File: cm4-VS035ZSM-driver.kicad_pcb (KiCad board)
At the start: 2 copper layers, 19 parts, among them U201 TPS65131RGE, U202 TLV62568DBV

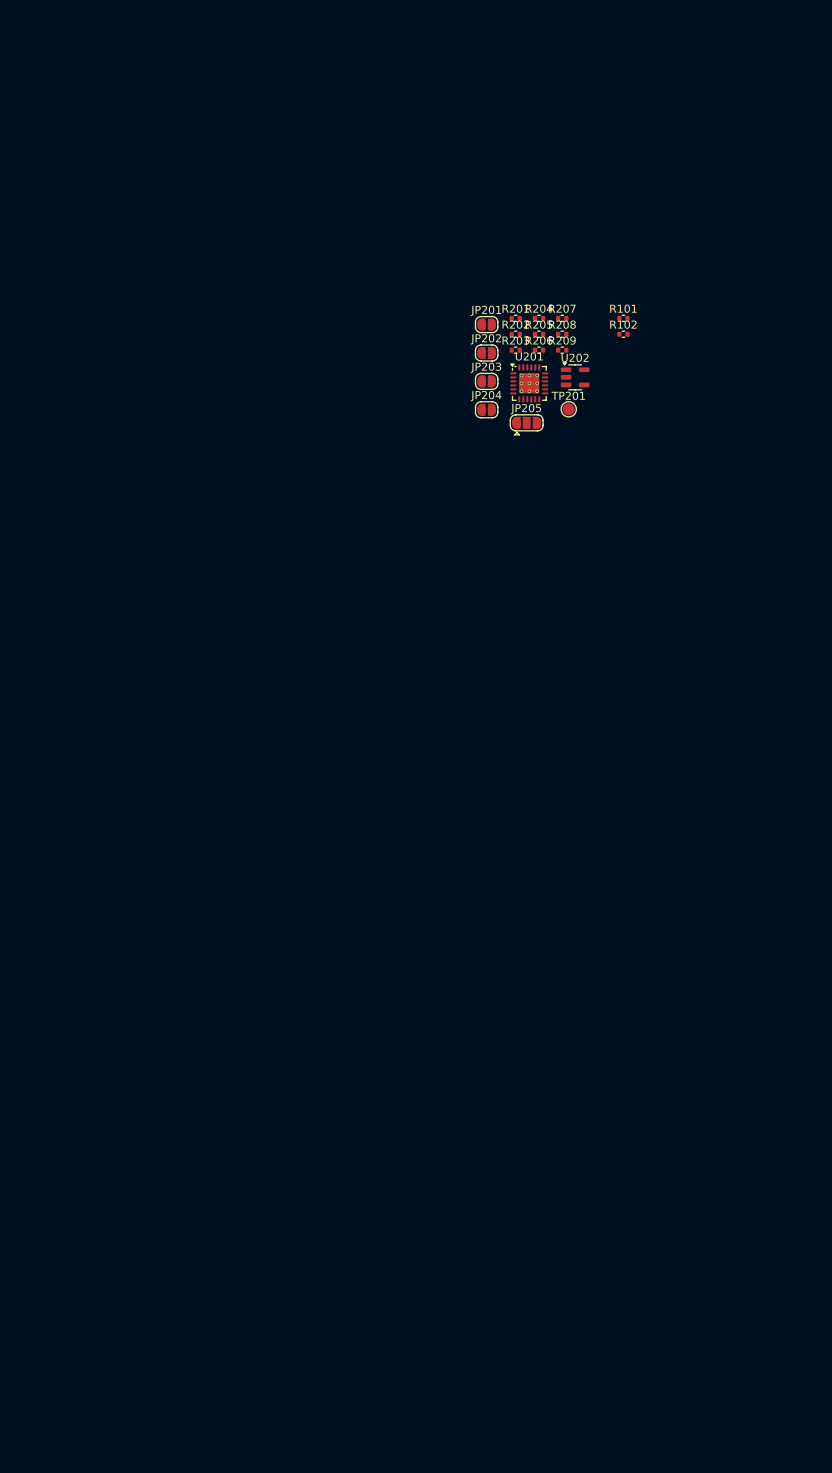
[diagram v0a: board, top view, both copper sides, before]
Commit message: 1v8 buck and 4.7uh inductor
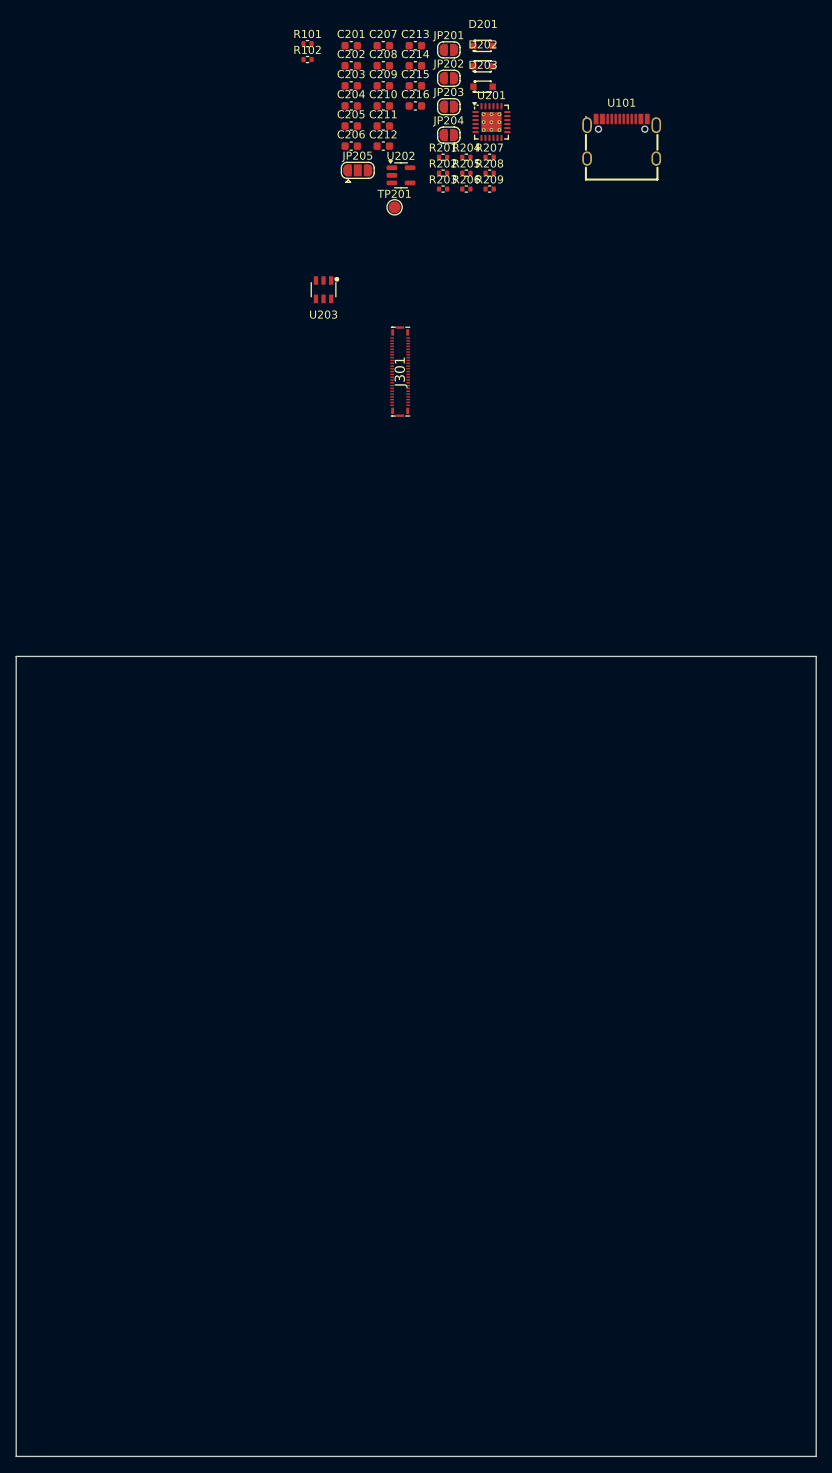
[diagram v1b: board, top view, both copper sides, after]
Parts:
- added C201: 10uF/25V, Capacitor_SMD:C_0603_1608Metric, F.Cu at (114.3, 44.3)
- added C202: 1uF/25V, Capacitor_SMD:C_0603_1608Metric, F.Cu at (114.3, 46.8)
- added C203: 10pF/25V, Capacitor_SMD:C_0603_1608Metric, F.Cu at (114.3, 49.3)
- added C204: 10uF/25V, Capacitor_SMD:C_0603_1608Metric, F.Cu at (114.3, 51.8)
- added C205: 10uF/25V, Capacitor_SMD:C_0603_1608Metric, F.Cu at (114.3, 54.4)
- added C206: 1uF/25V, Capacitor_SMD:C_0603_1608Metric, F.Cu at (114.3, 56.9)
- added C207: 10pF/25V, Capacitor_SMD:C_0603_1608Metric, F.Cu at (118.3, 44.3)
- added C208: 4.7nF/50V, Capacitor_SMD:C_0603_1608Metric, F.Cu at (118.3, 46.8)
- added C209: 10nF/25V, Capacitor_SMD:C_0603_1608Metric, F.Cu at (118.3, 49.3)
- added C210: 10uF/25V, Capacitor_SMD:C_0603_1608Metric, F.Cu at (118.3, 51.8)
- added C211: 10uF/25V, Capacitor_SMD:C_0603_1608Metric, F.Cu at (118.3, 54.4)
- added C212: 10uF/25V, Capacitor_SMD:C_0603_1608Metric, F.Cu at (118.3, 56.9)
- added C213: 6.8pF/10V, Capacitor_SMD:C_0603_1608Metric, F.Cu at (122.3, 44.3)
- added C214: 4.7uF/50V, Capacitor_SMD:C_0603_1608Metric, F.Cu at (122.3, 46.8)
- added C215: 2.2uF/50V, Capacitor_SMD:C_0603_1608Metric, F.Cu at (122.3, 49.3)
- added C216: 10uF/25V, Capacitor_SMD:C_0603_1608Metric, F.Cu at (122.3, 51.8)
- added D201: CUS10S40_H3F, footprints:SOD-323_L1.7-W1.3-LS2.5-RD, F.Cu at (130.7, 44.3)
- added D202: CUS10S40_H3F, footprints:SOD-323_L1.7-W1.3-LS2.5-RD, F.Cu at (130.7, 46.9)
- added D203: CUS10S40_H3F, footprints:SOD-323_L1.7-W1.3-LS2.5-RD, F.Cu at (130.7, 49.4)
- added J301: 245863050104829+, footprints:245863050104829, F.Cu at (120.4, 85.0)
- added U101: USB-TYPE-C-018, footprints:USB-C_SMD-TYPE-C-31-M-12, F.Cu at (148.1, 55.9)
- added U203: LP3320B6F, footprints:SOT-23-6_L2.9-W1.6-P0.95-LS2.8-BL, F.Cu at (110.8, 74.8)
- moved R101 52.3 mm to (108.8, 44.0)
- moved R102 52.3 mm to (108.8, 46.0)
- moved JP205 38.0 mm to (115.1, 59.9)
- moved JP201 34.7 mm to (126.5, 44.8)
- moved JP202 34.7 mm to (126.5, 48.4)
- moved JP203 34.7 mm to (126.5, 51.9)
- moved JP204 34.7 mm to (126.5, 55.5)
- moved TP201 33.3 mm to (119.7, 64.5)
- moved U202 33.3 mm to (120.5, 60.5)
- moved U201 33.0 mm to (131.8, 53.9)
- moved R203 22.1 mm to (125.8, 62.2)
- moved R206 22.1 mm to (128.7, 62.2)
- moved R209 22.1 mm to (131.6, 62.2)
- moved R201 22.1 mm to (125.8, 58.2)
- moved R204 22.1 mm to (128.7, 58.2)
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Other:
- board outline added: 100 x 100 mm

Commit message: init layout
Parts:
- removed C201, C204, C205, C210, C211: 10uF/25V, Capacitor_SMD:C_0603_1608Metric
- removed C202, C206: 1uF/25V, Capacitor_SMD:C_0603_1608Metric
- removed C203, C207: 10pF/25V, Capacitor_SMD:C_0603_1608Metric
- removed C208: 4.7nF/50V, Capacitor_SMD:C_0603_1608Metric
- removed C209: 10nF/25V, Capacitor_SMD:C_0603_1608Metric
- removed D201, D202, D203: CUS10S40_H3F, footprints:SOD-323_L1.7-W1.3-LS2.5-RD
- removed JP201: Jumper-, Jumper:SolderJumper-2_P1.3mm_Open_RoundedPad1.0x1.5mm
- removed JP202: Jumper+, Jumper:SolderJumper-2_P1.3mm_Open_RoundedPad1.0x1.5mm
- removed R101, R102: 5.1K, Resistor_SMD:R_0402_1005Metric
- removed R201: 10Ω/1%, Resistor_SMD:R_0402_1005Metric
- removed R202: 560kΩ/1%, Resistor_SMD:R_0402_1005Metric
- removed R203, R204: 150kΩ/1%, Resistor_SMD:R_0402_1005Metric
- removed R205: 715kΩ/1%, Resistor_SMD:R_0402_1005Metric
- removed R206: 100kΩ/1%, Resistor_SMD:R_0402_1005Metric
- removed R207: 200KΩ/1%, Resistor_SMD:R_0402_1005Metric
- removed U101: USB-TYPE-C-018, footprints:USB-C_SMD-TYPE-C-31-M-12
- removed U201: TPS65131RGE, Package_DFN_QFN:VQFN-24-1EP_4x4mm_P0.5mm_EP2.45x2.45mm_ThermalVias
- added C220: 4.7uF/16V, Capacitor_SMD:C_0603_1608Metric, F.Cu at (180.6, 55.0)
- added C221: 4.7uF/16V, Capacitor_SMD:C_0603_1608Metric, F.Cu at (185.1, 49.8)
- added C222: 4.7uF/16V, Capacitor_SMD:C_0603_1608Metric, F.Cu at (181.6, 47.1)
- added C223: 4.7uF/16V, Capacitor_SMD:C_0603_1608Metric, F.Cu at (178.2, 50.5)
- added D403: B5817WS_C7420329, footprints:SOD-323_L1.7-W1.3-LS2.5-FD, F.Cu at (185.3, 61.8)
- added J302: Conn_01x22, footprints:CON22_1X22_DRB_XF2C_TYC, F.Cu at (195.9, 70.4)
- added J303: Conn_01x02_LCD_Breakout, Connector_PinHeader_2.54mm:PinHeader_1x02_P2.54mm_Vertical, F.Cu at (205.6, 65.9)
- added J304: Conn_01x04_power_jumpers, Connector_PinHeader_2.54mm:PinHeader_1x04_P2.54mm_Vertical, F.Cu at (209.2, 71.0)
- added JP208: +5.7_bridge, Connector_PinHeader_2.54mm:PinHeader_1x02_P2.54mm_Vertical, F.Cu at (181.2, 60.2)
- added JP209: -5v7_bridge, Connector_PinHeader_2.54mm:PinHeader_1x02_P2.54mm_Vertical, F.Cu at (177.6, 57.6)
- added JP210: Jumper+, Connector_PinHeader_2.54mm:PinHeader_1x02_P2.54mm_Vertical, F.Cu at (188.4, 47.1)
- added JP211: Jumper-, Connector_PinHeader_2.54mm:PinHeader_1x02_P2.54mm_Vertical, F.Cu at (188.4, 55.8)
- added L204: 4.7uH, footprints:IND-SMD_L2.5-W2.0_SPH252012, F.Cu at (181.8, 66.6)
- added L206: 4.7uH, footprints:IND-SMD_L2.5-W2.0_SPH252012, F.Cu at (201.8, 42.3)
- added L207: 4.7uH, footprints:IND-SMD_L2.5-W2.0_SPH252012, F.Cu at (177.8, 47.1)
- added NT201: NetTie_GND, NetTie:NetTie-2_SMD_Pad0.5mm, B.Cu at (183.4, 44.8)
- added TP203: TestPoint_GND_PAD, TestPoint:TestPoint_THTPad_D2.0mm_Drill1.0mm, F.Cu at (195.1, 43.4)
- added TP204: TestPoint_GNDA_PAD, TestPoint:TestPoint_THTPad_D2.0mm_Drill1.0mm, F.Cu at (185.0, 46.9)
- added TP205: TestPoint_anode, TestPoint:TestPoint_THTPad_D2.0mm_Drill1.0mm, F.Cu at (177.6, 63.8)
- added TP206: TestPoint_cathode, TestPoint:TestPoint_THTPad_D2.0mm_Drill1.0mm, F.Cu at (186.2, 67.1)
- added TP207: TestPoint_PWM, TestPoint:TestPoint_THTPad_D2.0mm_Drill1.0mm, F.Cu at (177.8, 67.0)
- added TP208: TestPoint_P_5V7, TestPoint:TestPoint_THTPad_D2.0mm_Drill1.0mm, F.Cu at (186.6, 43.1)
- added TP209: TestPoint_N_5V7, TestPoint:TestPoint_THTPad_D2.0mm_Drill1.0mm, F.Cu at (185.0, 55.7)
- added U204: MCP1603T-180I/OS, footprints:TSOT5_MC_MCH, F.Cu at (205.6, 42.0)
- C212: value 10uF/25V -> 4.7uF/16V
- C213: value 6.8pF/10V -> 2.2uF/50V; footprint Capacitor_SMD:C_0603_1608Metric -> Capacitor_SMD:C_0805_2012Metric
- C214: value 4.7uF/50V -> 4.7uF/16V
- C215: footprint Capacitor_SMD:C_0603_1608Metric -> Capacitor_SMD:C_0805_2012Metric
- J301: footprint footprints:245863050104829 -> footprints:245863050104829_missing pads
- JP203, JP204: footprint Jumper:SolderJumper-2_P1.3mm_Open_RoundedPad1.0x1.5mm -> Connector_PinHeader_2.54mm:PinHeader_1x02_P2.54mm_Vertical
- JP205: footprint Jumper:SolderJumper-3_P1.3mm_Open_RoundedPad1.0x1.5mm -> Connector_PinHeader_2.54mm:PinHeader_1x03_P2.54mm_Vertical
- TP201: footprint TestPoint:TestPoint_Pad_D1.5mm -> TestPoint:TestPoint_THTPad_D2.0mm_Drill1.0mm
- U202: value TLV62568DBV -> TPS65132WRVCR_C2876379; footprint Package_TO_SOT_SMD:SOT-23-5 -> footprints:WQFN-20_L4.0-W3.0-P0.50-BL-EP
- moved TP201 91.5 mm to (207.5, 39.0), turned to 180 degrees
- moved C212 86.4 mm to (202.9, 39.7), turned to 180 degrees
- moved C214 86.2 mm to (208.4, 42.7), turned to -90 degrees
- moved JP204 85.9 mm to (210.9, 39.8)
- moved J301 82.6 mm to (196.3, 52.6)
- moved U203 73.6 mm to (183.7, 64.7), turned to 45 degrees
- moved JP203 73.0 mm to (198.6, 40.9)
- moved JP205 69.6 mm to (183.8, 70.7), turned to -90 degrees
- moved C215 65.8 mm to (186.5, 63.9), turned to -45 degrees
- moved C213 62.8 mm to (184.6, 52.2), turned to 90 degrees
- moved U202 61.5 mm to (181.2, 51.2), turned to -90 degrees
- moved C216 59.6 mm to (180.6, 64.1), turned to 45 degrees
- moved R209 55.7 mm to (186.6, 70.7), turned to 90 degrees
- moved R208 52.5 mm to (184.0, 61.1), turned to -135 degrees
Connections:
- net +5V renamed +3V3
- C213 pad 1: Net-(JP203-A) -> Net-(U202-CFLY2)
- C213 pad 2: Net-(U202-FB) -> Net-(U202-CFLY1)
- J301 pad 41: /high-speed/LED_PWR.A -> /MIPI-screen/LED_PWR.A
- J301 pad 45: /high-speed/LED_PWR.K -> /MIPI-screen/LED_PWR.K
- J301 pad 47: /high-speed/LED_PWR.K -> /MIPI-screen/LED_PWR.K
- J301 pad 48: /high-speed/LED_PWR.PWM -> /MIPI-screen/LED_PWR.PWM
- U202 pad 1: Net-(JP204-A) -> GND
- U202 pad 3: Net-(U202-SW) -> GNDA
- U202 pad 5: Net-(U202-FB) -> Net-(JP208-B)
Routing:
- net /high-speed/DSI0_DATA.3_N: track 0.00 -> 26.7 mm
- net /high-speed/DSI0_DATA.2_N: track 0.00 -> 26.5 mm
- net /high-speed/DSI0_DATA.0_N: track 0.00 -> 26.5 mm
- net /high-speed/DSI0_DATA.1_N: track 0.00 -> 26.5 mm
- net /high-speed/DSI0_CLK.N: track 0.00 -> 26.5 mm
- net /high-speed/DSI0_DATA.0_P: track 0.00 -> 26.2 mm
- net /high-speed/DSI0_DATA.1_P: track 0.00 -> 26.2 mm
- net /high-speed/DSI0_DATA.2_P: track 0.00 -> 26.0 mm
- net /high-speed/DSI0_CLK.P: track 0.00 -> 26.0 mm
- net /high-speed/DSI0_DATA.3_P: track 0.00 -> 25.6 mm
- net +3V3: track 0.00 -> 11.4 mm
- net GND: track 0.00 -> 7.66 mm
- net Net-(JP203-A): track 0.00 -> 4.16 mm
- net Net-(U202-CFLY2): track 0.00 -> 3.72 mm
- net /MIPI-screen/OUTP: track 0.00 -> 3.47 mm
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- added copper zone on F.Cu, net /MIPI-screen/SW
- added copper zone on B.Cu, net GND
- added copper zone on F.Cu, net GND
- added copper zone on In1.Cu, net GND
- added copper zone on In2.Cu, net GND
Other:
- board size 100 x 100 mm -> 37.6 x 35.5 mm
- copper layers 2 -> 4
- board text added: "good luck!"
- board text added: "it might be facing this way"

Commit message: silkscreen
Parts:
- added kibuzzard-685CA5E3: G***, kibuzzard-685CA5E3, F.Cu at (169.8, 57.6)
- added kibuzzard-685CA5ED: G***, kibuzzard-685CA5ED, F.Cu at (169.7, 59.6)
- added kibuzzard-685CA646: G***, kibuzzard-685CA646, F.Cu at (170.3, 62.0)
- added kibuzzard-685CA653: G***, kibuzzard-685CA653, F.Cu at (170.0, 64.1)
- added kibuzzard-685CA659: G***, kibuzzard-685CA659, F.Cu at (170.1, 65.8)
- added kibuzzard-685CA68D: G***, kibuzzard-685CA68D, F.Cu at (171.1, 50.6)
- added kibuzzard-685CA698: G***, kibuzzard-685CA698, F.Cu at (170.9, 48.8)
- added kibuzzard-685CA6CA: G***, kibuzzard-685CA6CA, F.Cu at (170.6, 42.8)
- added kibuzzard-685CA6D3: G***, kibuzzard-685CA6D3, F.Cu at (170.4, 41.0)
- added kibuzzard-685CA6E7: G***, kibuzzard-685CA6E7, F.Cu at (170.7, 34.7)
- added kibuzzard-685CA70B: G***, kibuzzard-685CA70B, F.Cu at (193.1, 36.0)
- added kibuzzard-685CA724: G***, kibuzzard-685CA724, F.Cu at (200.3, 36.0)
- added kibuzzard-685CA72C: G***, kibuzzard-685CA72C, F.Cu at (208.8, 36.2)
- moved TP201 12.6 mm to (195.0, 40.0)
- moved J303 4.55 mm to (209.5, 63.5)
- moved C213 3.87 mm to (184.6, 48.3)
- moved C222 3.87 mm to (181.6, 43.2)
- moved C220 3.87 mm to (180.6, 51.1)
- moved C221 3.87 mm to (185.1, 45.9)
- moved C223 3.87 mm to (178.2, 46.7)
- moved JP208 3.87 mm to (181.2, 56.3)
- moved JP209 3.87 mm to (177.6, 53.8)
- moved JP210 3.87 mm to (188.4, 43.2)
- moved JP211 3.87 mm to (188.4, 51.9)
- moved L207 3.87 mm to (177.8, 43.2)
- moved NT201 3.87 mm to (183.4, 40.9)
- moved TP204 3.87 mm to (185.0, 43.1)
- moved TP209 3.87 mm to (185.0, 51.8)
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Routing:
- net /high-speed/DSI0_DATA.3_P: track 25.6 -> 26.6 mm

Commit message: board fabbed
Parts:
- removed J303: Conn_01x02_LCD_Breakout, Connector_PinHeader_2.54mm:PinHeader_1x02_P2.54mm_Vertical
- removed R208: 100KΩ/1%, Resistor_SMD:R_0402_1005Metric
- added G***: LOGO, custom-graphics:isaac-anime-girl-2, F.Cu at (204.3, 47.9)
- added H305: MountingHole_Pad, MountingHole:MountingHole_3.2mm_M3_DIN965_Pad_TopBottom, F.Cu at (179.0, 37.5)
- added H307: MountingHole_Pad, MountingHole:MountingHole_3.2mm_M3_DIN965_Pad_TopBottom, F.Cu at (205.2, 36.7)
- added H308: MountingHole_Pad, MountingHole:MountingHole_3.2mm_M3_DIN965_Pad_TopBottom, F.Cu at (209.6, 70.0)
- added J305: Conn_01x03_Pin, Connector_PinHeader_2.54mm:PinHeader_1x03_P2.54mm_Vertical, F.Cu at (204.3, 64.8)
- added R206: 5.1Ω/1%, Resistor_SMD:R_0805_2012Metric, F.Cu at (179.6, 64.6)
- added R301: 2.2kΩ, Resistor_SMD:R_0402_1005Metric, F.Cu at (184.3, 59.1)
- added R302: 2.2kΩ, Resistor_SMD:R_0402_1005Metric, F.Cu at (187.0, 57.3)
- added R303: 2.2kΩ, Resistor_SMD:R_0402_1005Metric, F.Cu at (204.9, 71.5)
- added R304: 2.7kΩ, Resistor_SMD:R_0603_1608Metric, F.Cu at (204.7, 69.4)
- added REF**: sus-microsystems_amogus, custom-graphics:sus-microsystems_amogus, F.Cu at (194.0, 44.9)
- added REF**: sus-microsystems_amogus, custom-graphics:sus-microsystems_amogus, F.Cu at (184.0, 38.6)
- added kibuzzard-685CA5E3: G***, kibuzzard-685CA5E3, B.Cu at (186.9, 65.6)
- added kibuzzard-685CA5ED: G***, kibuzzard-685CA5ED, B.Cu at (183.5, 59.4)
- added kibuzzard-685CA646: G***, kibuzzard-685CA646, B.Cu at (180.2, 71.6)
- added kibuzzard-685CA653: G***, kibuzzard-685CA653, B.Cu at (177.6, 69.7)
- added kibuzzard-685CA659: G***, kibuzzard-685CA659, B.Cu at (182.8, 69.6)
- added kibuzzard-685CA68D: G***, kibuzzard-685CA68D, B.Cu at (177.2, 54.9)
- added kibuzzard-685CA698: G***, kibuzzard-685CA698, B.Cu at (184.6, 55.0)
- added kibuzzard-685CA6CA: G***, kibuzzard-685CA6CA, B.Cu at (189.4, 52.6)
- added kibuzzard-685CA6D3: G***, kibuzzard-685CA6D3, B.Cu at (186.5, 41.7)
- added kibuzzard-685CA6E7: G***, kibuzzard-685CA6E7, B.Cu at (181.2, 42.8)
- added kibuzzard-685CA70B: G***, kibuzzard-685CA70B, B.Cu at (194.6, 43.1)
- added kibuzzard-685CA724: G***, kibuzzard-685CA724, B.Cu at (200.0, 42.2)
- added kibuzzard-685CA72C: G***, kibuzzard-685CA72C, B.Cu at (209.5, 46.6)
- added kibuzzard-68620294: G***, kibuzzard-68620294, F.Cu at (204.2, 58.8)
- added kibuzzard-68620294: G***, kibuzzard-68620294, B.Cu at (204.1, 59.0)
- added kibuzzard-686202AB: G***, kibuzzard-686202AB, F.Cu at (209.8, 58.8)
- added kibuzzard-686202AB: G***, kibuzzard-686202AB, F.Cu at (192.3, 43.6)
- added kibuzzard-686202AB: G***, kibuzzard-686202AB, B.Cu at (209.4, 59.0)
- added kibuzzard-686202AB: G***, kibuzzard-686202AB, B.Cu at (191.7, 37.6)
- added kibuzzard-686202C6: G***, kibuzzard-686202C6, F.Cu at (202.1, 64.9)
- added kibuzzard-686202C6: G***, kibuzzard-686202C6, B.Cu at (202.4, 64.7)
- added kibuzzard-686202CD: G***, kibuzzard-686202CD, F.Cu at (205.7, 67.2)
- added kibuzzard-686202CD: G***, kibuzzard-686202CD, B.Cu at (206.8, 62.9)
- added kibuzzard-68621440: G***, kibuzzard-68621440, F.Cu at (211.7, 65.0)
- added kibuzzard-68621440: G***, kibuzzard-68621440, B.Cu at (211.4, 64.8)
- added kibuzzard-68621EB5: G***, kibuzzard-68621EB5, F.Cu at (197.0, 36.4)
- added kibuzzard-68622B0B: G***, kibuzzard-68622B0B, B.Cu at (195.7, 50.2)
- added kibuzzard-68622B1B: G***, kibuzzard-68622B1B, B.Cu at (200.7, 51.0)
- NT201: moved to F.Cu
- moved kibuzzard-685CA6CA 20.9 mm to (189.9, 50.8), turned to -90 degrees
- moved kibuzzard-685CA6D3 20.8 mm to (190.9, 44.5), turned to -90 degrees
- moved kibuzzard-685CA5E3 18.8 mm to (187.0, 65.3)
- moved kibuzzard-685CA5ED 17.4 mm to (187.0, 61.3)
- moved kibuzzard-685CA698 15.5 mm to (185.2, 54.9), turned to -90 degrees
- moved kibuzzard-685CA6E7 15.2 mm to (184.6, 40.8)
- moved kibuzzard-685CA646 14.1 mm to (180.5, 71.7)
- moved kibuzzard-685CA659 13.6 mm to (183.0, 70.2)
- moved TP207 11.1 mm to (186.3, 70.8)
- moved J304 11.0 mm to (210.7, 61.2), turned to -90 degrees
- moved kibuzzard-685CA653 9.93 mm to (177.9, 70.2)
- moved kibuzzard-685CA72C 9.87 mm to (209.8, 46.0)
- moved TP205 9.46 mm to (186.9, 59.2)
- moved kibuzzard-685CA68D 7.27 mm to (176.9, 55.1), turned to 90 degrees
- moved kibuzzard-685CA70B 7.23 mm to (194.8, 43.0)
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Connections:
- J301 pad 42: /high-speed/LCD_RST -> LCD_RESET_DISPLAY_SIDE
- J301 pad 48: /MIPI-screen/LED_PWR.PWM -> LCD_CONNECTOR_PWM
- J302 pad 18: LED_EN -> LED_PWM
- J304 pad 3: +3V3 -> +1V8
- J304 pad 4: +3V3 -> +1V8
- JP205 pad 1: /MIPI-screen/LED_PWR.PWM -> LED_PWM
- R209 pad 1: /MIPI-screen/LED_PWR.PWM -> LED_PWM
- TP207 pad 1: /MIPI-screen/LED_PWR.PWM -> LED_PWM
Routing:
- net +3V3: track 11.4 -> 98.4 mm, vias 0 -> 2
- net SCL_3V3: track 0.00 -> 33.8 mm, vias 0 -> 3
- net SDA_3V3: track 0.00 -> 32.2 mm, vias 0 -> 3
- net +1V8: track 0.00 -> 28.8 mm
- net LCD_RESET_DISPLAY_SIDE: track 0.00 -> 25.8 mm, vias 0 -> 1
- net LCD_CONNECTOR_PWM: track 0.00 -> 24.0 mm, vias 0 -> 1
- net LED_PWM: track 0.00 -> 21.3 mm, vias 0 -> 1
- net /high-speed/TE: track 0.00 -> 19.6 mm, vias 0 -> 1
- net /MIPI-screen/LED_PWR.K: track 3.07 -> 19.5 mm
- net /MIPI-screen/LED_PWR.A: track 2.31 -> 15.3 mm
- net /MIPI-screen/OUTN: track 1.94 -> 11.6 mm
- net /MIPI-screen/OUTP: track 3.47 -> 12.1 mm
- net /MIPI-screen/BACKLIGHT_EN: track 1.77 -> 10.2 mm, vias 0 -> 1
- net Net-(JP208-B): track 1.07 -> 9.24 mm
- net +5V7: track 0.00 -> 8.17 mm
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- added copper zone on F.Cu, net +1V8
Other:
- board size 37.6 x 35.5 mm -> 38 x 40 mm
- board text added: "VS035ZSM MIPI Driver By Vincent Xie"
- board text added: "hello! hello! hello!"
